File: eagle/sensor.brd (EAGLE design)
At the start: 100 x 80 mm, 8 parts, among them IC1 LM358N, X1 1503_02, X2 0-Vcc

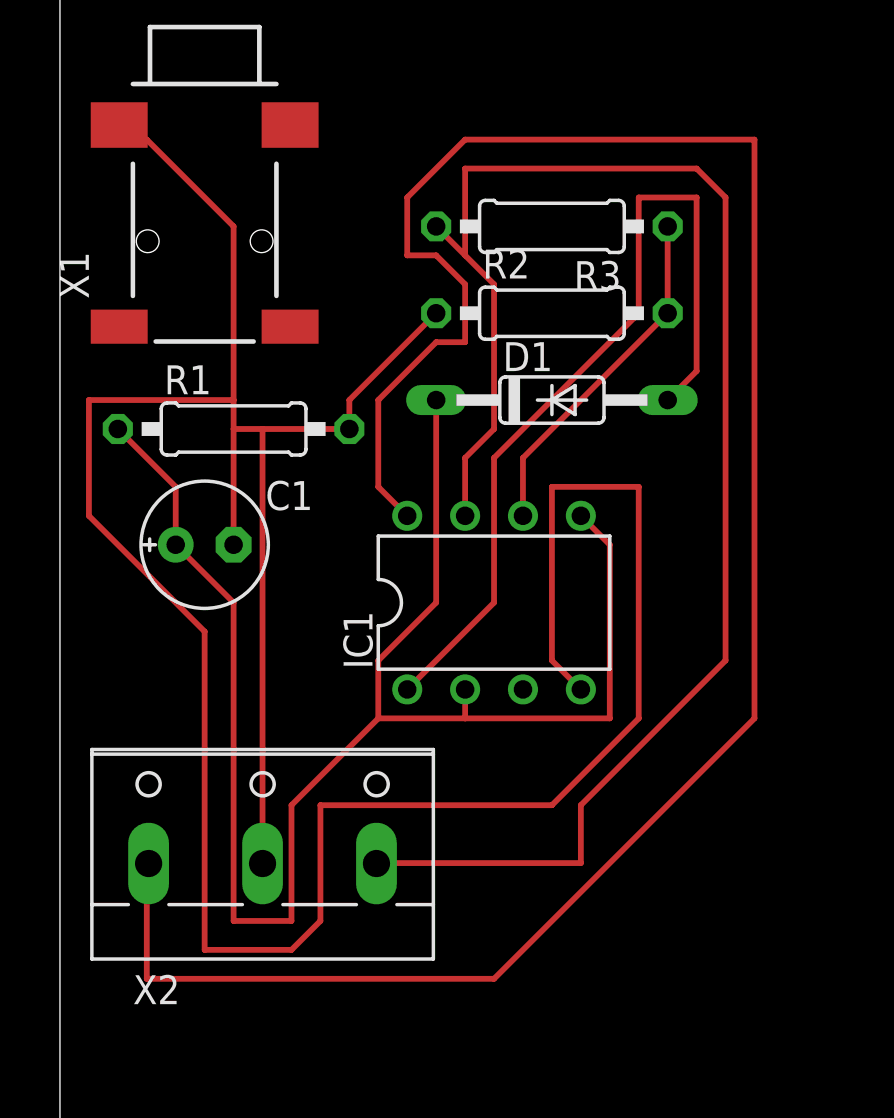
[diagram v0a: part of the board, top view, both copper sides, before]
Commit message: Rerouted board for two layer print.
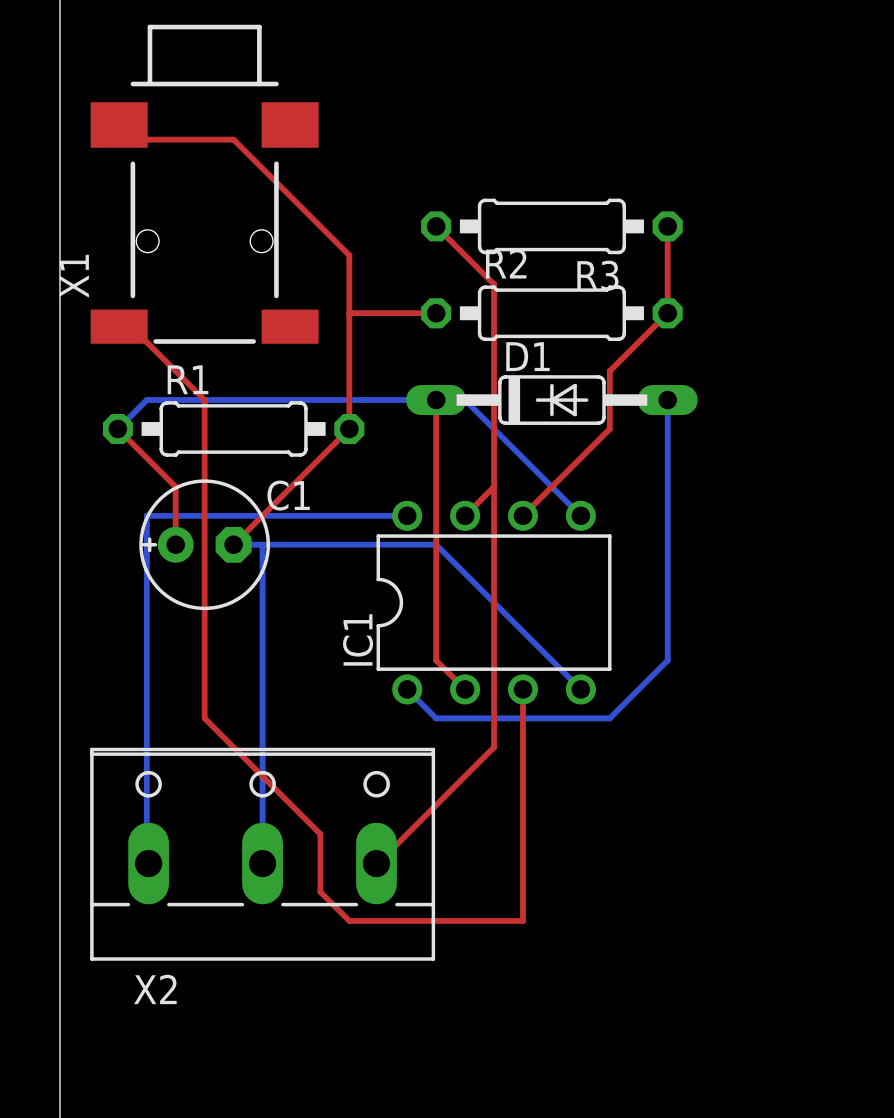
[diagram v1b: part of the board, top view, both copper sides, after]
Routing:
- net 0V: track 133.7 -> 62.8 mm
- net VCC: track 96.8 -> 26.8 mm
- net N$8: track 0.00 -> 48.3 mm
- net N$5: track 70.9 -> 33.0 mm
- net N$1: track 72.6 -> 42.3 mm
- net N$3: track 37.8 -> 24.4 mm

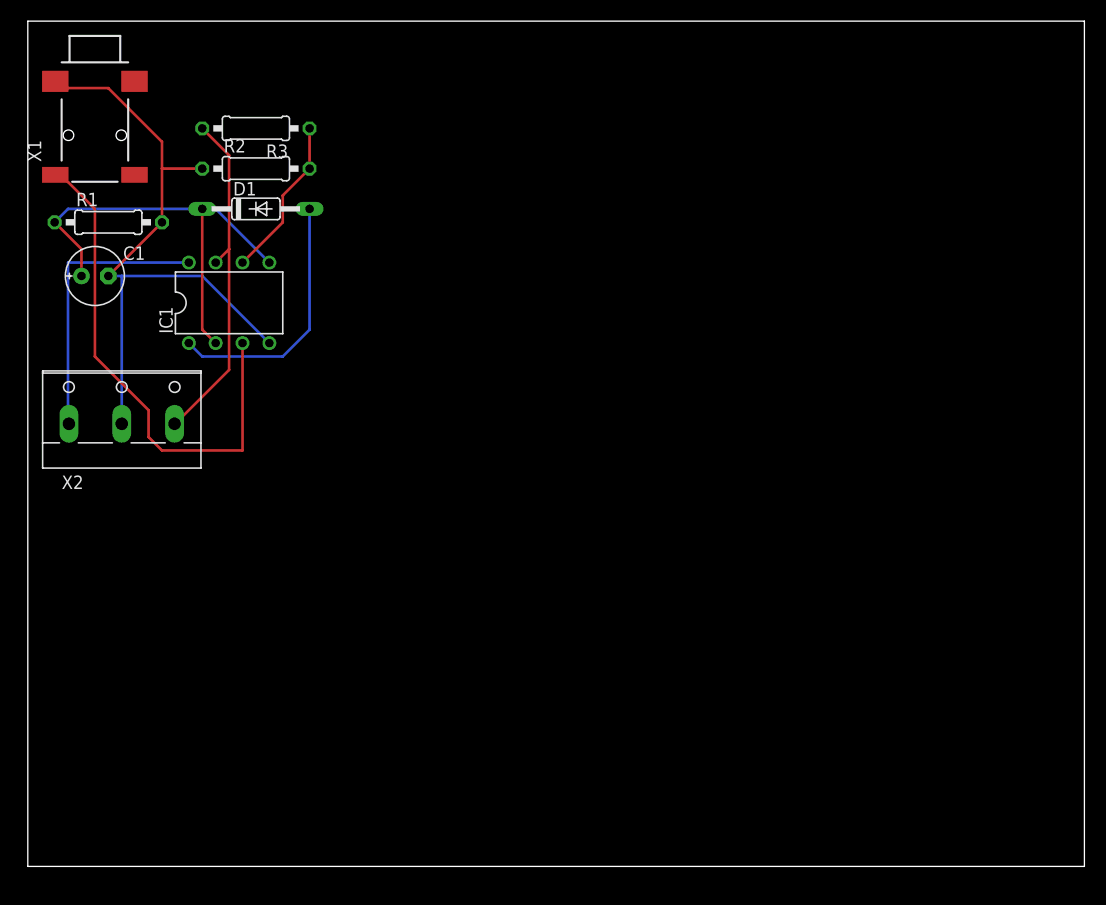
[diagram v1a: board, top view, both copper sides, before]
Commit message: reduce board size
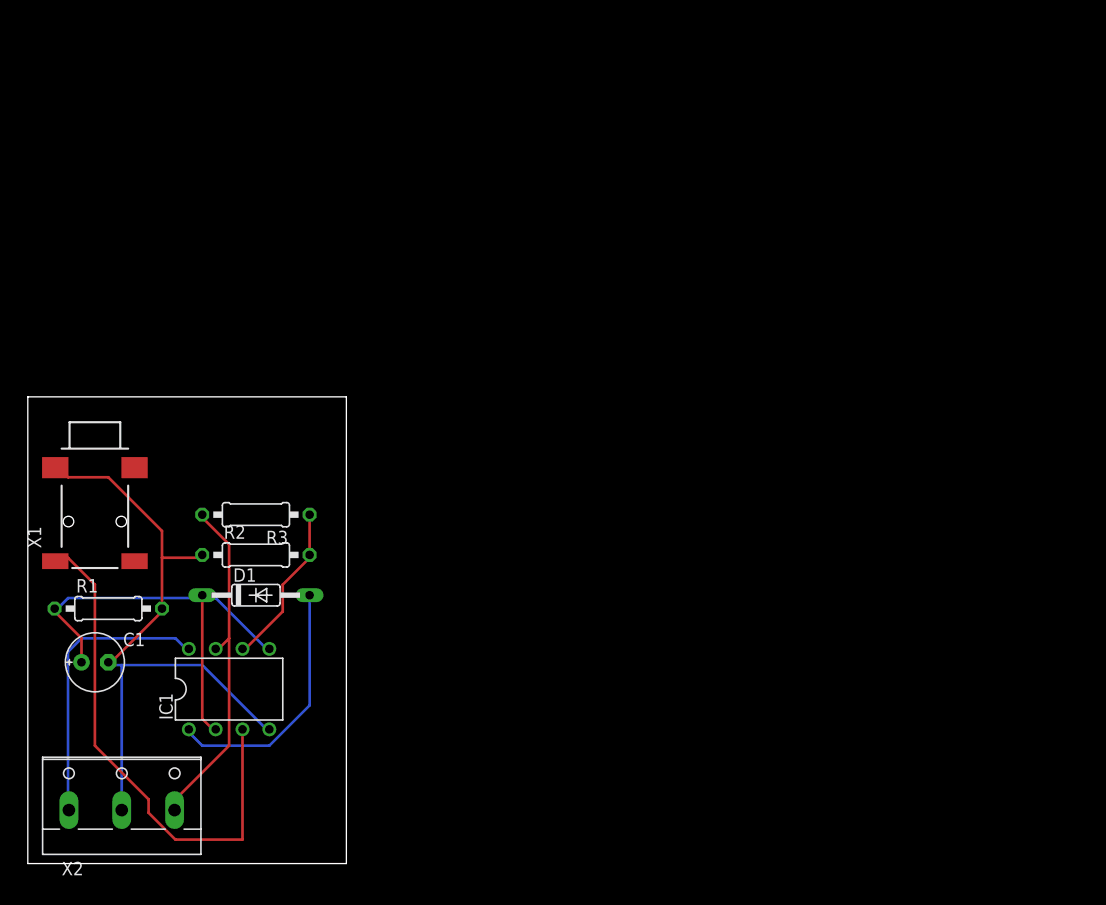
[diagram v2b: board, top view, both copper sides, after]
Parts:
- D1: value 1N4148DO35-10 -> 1N4148
- moved C1 36.6 mm to (6.35, 19.3)
- moved IC1 36.6 mm to (19.1, 16.8)
- moved R1 36.6 mm to (7.62, 24.4)
- moved R2 36.6 mm to (21.6, 29.5)
- moved X1 36.6 mm to (6.35, 39.6)
- moved X2 36.6 mm to (8.89, 6.62)
- moved D1 36.6 mm to (21.6, 25.7)
- moved R3 36.6 mm to (21.6, 33.3)
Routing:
- net N$1: track 42.3 -> 43.9 mm
- net VCC: track 26.8 -> 27.7 mm
- net 0V: track 62.8 -> 63.8 mm
- net N$8: track 48.3 -> 48.9 mm
- net N$2: track 15.3 -> 15.9 mm
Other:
- board size 100 x 80 mm -> 30.1 x 44.2 mm
